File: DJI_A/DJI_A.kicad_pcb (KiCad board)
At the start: 2 copper layers, 41.7 x 34.9 mm, 3 parts, among them J1 Conn_01x26, J2 Conn_01x26, J3 Conn_02x13_Odd_Even

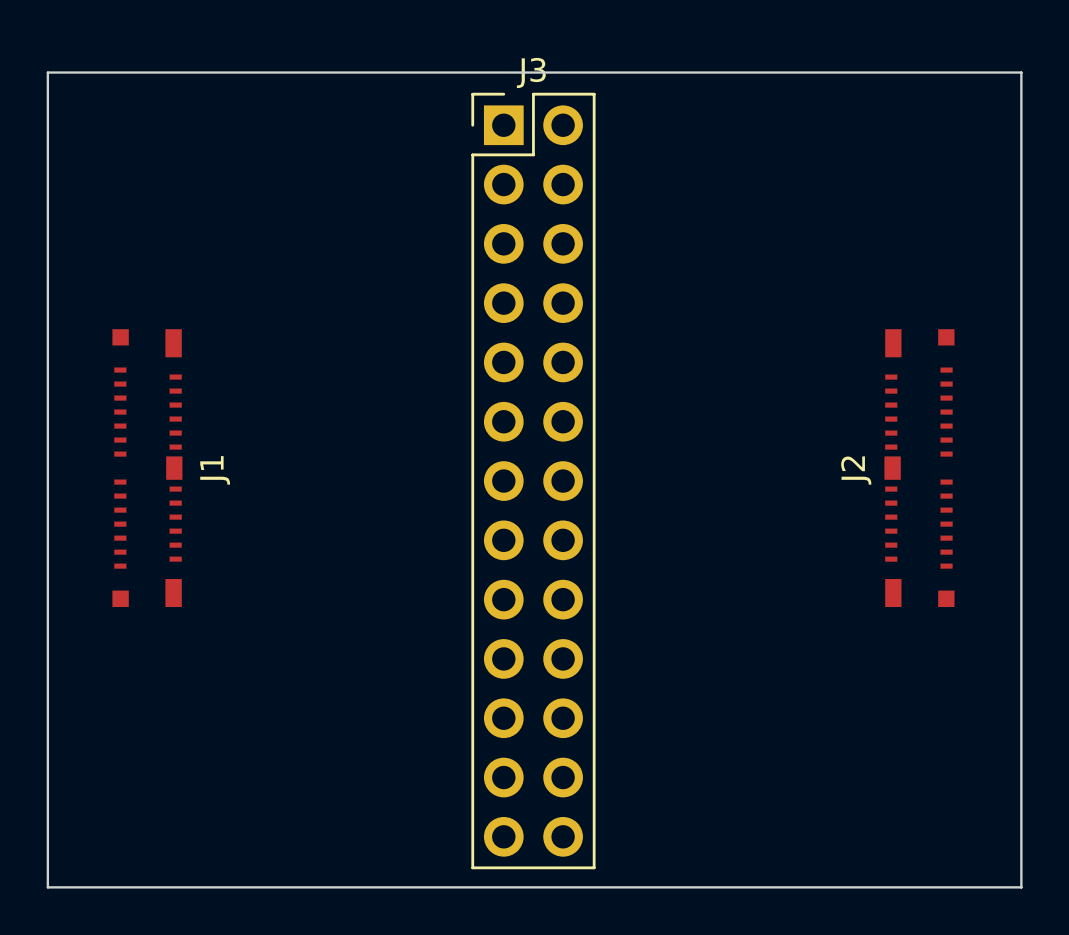
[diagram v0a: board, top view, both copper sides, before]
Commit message: Possible straight-through pinout. Don't use this version.
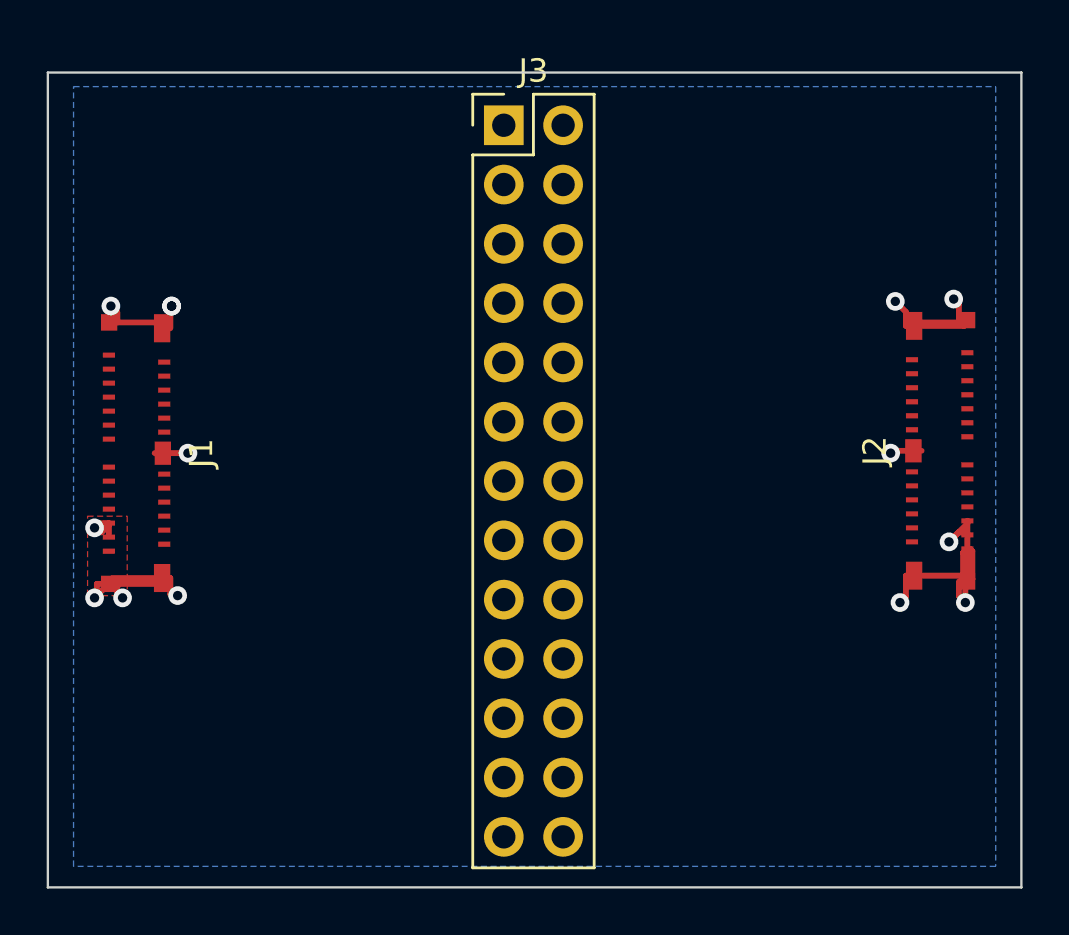
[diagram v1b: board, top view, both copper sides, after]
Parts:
- J1: value Conn_01x26 -> To Cam
- J2: value Conn_01x26 -> To Air Unit
- moved J2 1.16 mm to (68.2, 39.9)
- moved J1 0.81 mm to (33.8, 40.0)
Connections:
- J1 pad 22: Net-(J1-Pad22) -> GND
- J1 pad 24: Net-(J1-Pad24) -> GND
- J1 pad 26: Net-(J1-Pad26) -> GND
- J1 pad GND: (no net) -> GND
- J2 pad 1: Net-(J1-Pad26) -> GND
- J2 pad 3: Net-(J1-Pad24) -> GND
- J2 pad 5: Net-(J1-Pad22) -> GND
- J2 pad GND: (no net) -> GND
- J3 pad 22: Net-(J1-Pad22) -> GND
- J3 pad 24: Net-(J1-Pad24) -> GND
- J3 pad 26: Net-(J1-Pad26) -> GND
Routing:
- net GND: track 0.00 -> 38.0 mm, vias 0 -> 14
- added copper zone on B.Cu, net GND
- added copper zone on F.Cu, net GND
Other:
- board text added: "This layout is based on preliminary photos of a DJI board may not be valid in the case of crossover cable layout"
